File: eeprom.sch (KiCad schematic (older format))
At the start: 7 parts

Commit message: finalize schematic and PCB
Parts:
- added D3: LED, LED_SMD:LED_0603_1608Metric_Pad1.05x0.95mm_HandSolder, symbol Device:LED
- added D4: D_Schottky, Diode_SMD:D_0603_1608Metric_Pad1.05x0.95mm_HandSolder, symbol Device:D_Schottky
- added F2: Fuse, Fuse:Fuse_0603_1608Metric_Pad1.05x0.95mm_HandSolder, symbol Device:Fuse
- added R31: R, Resistor_SMD:R_0603_1608Metric_Pad1.05x0.95mm_HandSolder, symbol Device:R
- U10: renamed from U?; footprint Package_DFN_QFN:DFN-8-1EP_2x3mm_P0.5mm_EP0.61x2.2mm -> Package_DFN_QFN:DFN-8-1EP_3x2mm_P0.5mm_EP1.75x1.45mm
- gave numbers to parts that had none: 6
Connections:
- net labels added: 5V_IN_RAW
- net labels removed: 5V_IN
- wire segments 24 -> 29
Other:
- moved on the sheet: C35, R32, R33, R34, R35, R36, U10

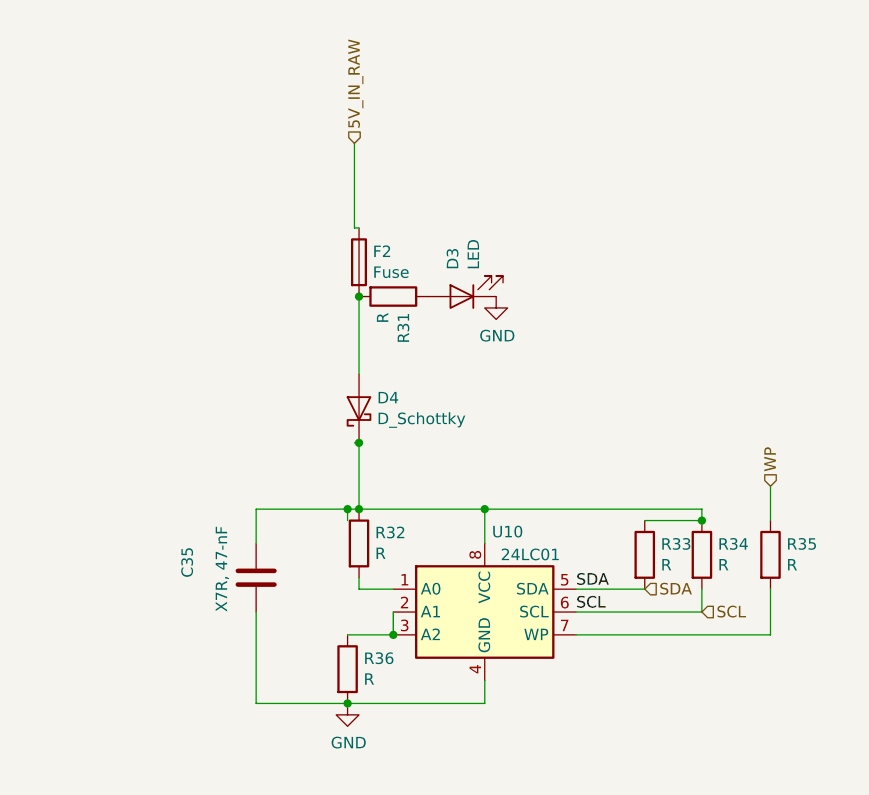
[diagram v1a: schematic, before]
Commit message: re route pcb-re arrange schematics
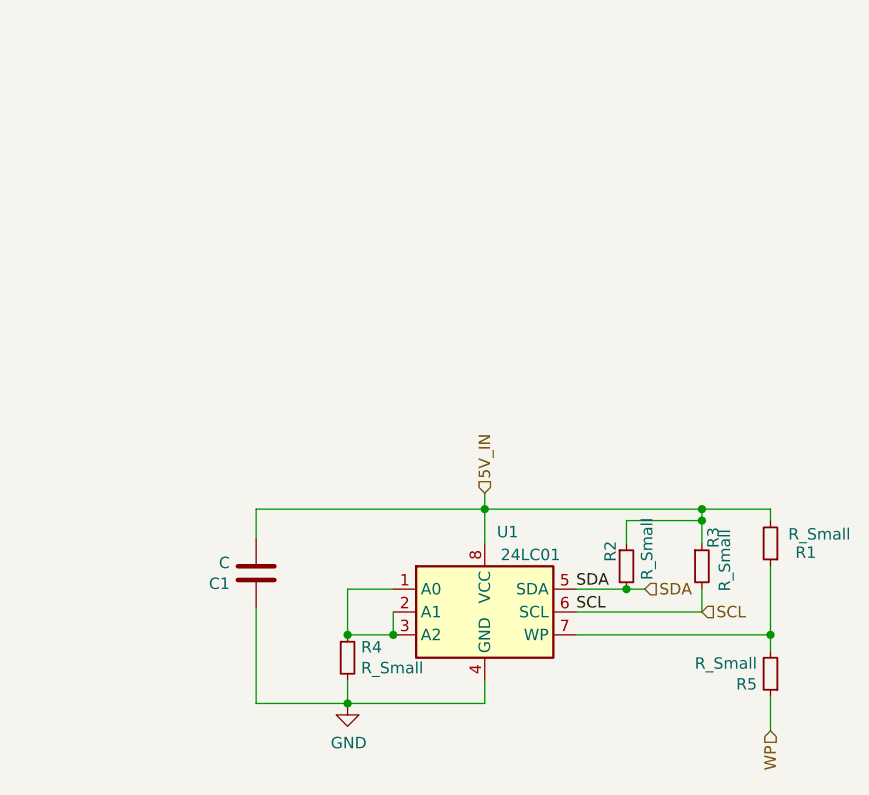
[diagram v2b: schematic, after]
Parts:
- removed C35: X7R, 47-nF, Capacitor_SMD:C_0603_1608Metric_Pad1.05x0.95mm_HandSolder, symbol Device:C
- removed D3: LED, LED_SMD:LED_0603_1608Metric_Pad1.05x0.95mm_HandSolder, symbol Device:LED
- removed D4: D_Schottky, Diode_SMD:D_0603_1608Metric_Pad1.05x0.95mm_HandSolder, symbol Device:D_Schottky
- removed F2: Fuse, Fuse:Fuse_0603_1608Metric_Pad1.05x0.95mm_HandSolder, symbol Device:Fuse
- removed R31, R32, R33, R34, R35, R36: R, Resistor_SMD:R_0603_1608Metric_Pad1.05x0.95mm_HandSolder, symbol Device:R
- added C1: C, Capacitor_SMD:C_0402_1005Metric, symbol Device:C
- added R1, R2, R3, R4, R5: R_Small, Resistor_SMD:R_0402_1005Metric, symbol Device:R_Small
- renumbered U10 to U1
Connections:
- net labels added: 5V_IN
- net labels removed: 5V_IN_RAW
- wire segments 29 -> 28
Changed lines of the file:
@@
 $Descr A4 11693 8268
 encoding utf-8
-Sheet 2 2
+Sheet 2 4
 Title ""
 Date ""
@@
 $EndDescr
 $Comp
-L Memory_EEPROM:24LC01 U10
+L Memory_EEPROM:24LC01 U1
 U 1 1 60F67DC6
 P 5000 4320
-F 0 "U10" H 5100 4670 50  0000 C CNN
+F 0 "U1" H 5100 4670 50  0000 C CNN
 F 1 "24LC01" H 5200 4570 50  0000 C CNN
 F 2 "Package_DFN_QFN:DFN-8-1EP_3x2mm_P0.5mm_EP1.75x1.45mm" H 5000 4320 50  0001 C CNN
@@
 	1    0    0    -1
 $EndComp
-$Comp
-L Device:R R32
-U 1 1 60F67DCC
-P 4450 4020
-F 0 "R32" H 4520 4066 50  0000 L CNN
-F 1 "R" H 4520 3975 50  0000 L CNN
-F 2 "Resistor_SMD:R_0603_1608Metric_Pad1.05x0.95mm_HandSolder" V 4380 4020 50  0001 C CNN
-F 3 "~" H 4450 4020 50  0001 C CNN
-	1    4450 4020
-	1    0    0    -1
-$EndComp
-Wire Wire Line
-	4600 4220 4450 4220
-Wire Wire Line
-	4450 4220 4450 4170
 Wire Wire Line
 	4600 4320 4600 4420
@@
 Connection ~ 4600 4420
 $Comp
-L Device:R R36
-U 1 1 60F67DD8
-P 4400 4570
-F 0 "R36" H 4470 4616 50  0000 L CNN
-F 1 "R" H 4470 4525 50  0000 L CNN
-F 2 "Resistor_SMD:R_0603_1608Metric_Pad1.05x0.95mm_HandSolder" V 4330 4570 50  0001 C CNN
-F 3 "~" H 4400 4570 50  0001 C CNN
-	1    4400 4570
-	1    0    0    -1
-$EndComp
-$Comp
-L power:GND #PWR020
+L power:GND #PWR01
 U 1 1 60F67DDE
 P 4400 4720
-F 0 "#PWR020" H 4400 4470 50  0001 C CNN
+F 0 "#PWR01" H 4400 4470 50  0001 C CNN
 F 1 "GND" H 4405 4547 50  0000 C CNN
 F 2 "" H 4400 4720 50  0001 C CNN
@@
 	1    0    0    -1
 $EndComp
-$Comp
-L Device:R R33
-U 1 1 60F67DE4
-P 5700 4070
-F 0 "R33" H 5770 4116 50  0000 L CNN
-F 1 "R" H 5770 4025 50  0000 L CNN
-F 2 "Resistor_SMD:R_0603_1608Metric_Pad1.05x0.95mm_HandSolder" V 5630 4070 50  0001 C CNN
-F 3 "~" H 5700 4070 50  0001 C CNN
-	1    5700 4070
-	1    0    0    -1
-$EndComp
-$Comp
-L Device:R R34
-U 1 1 60F67DEA
-P 5950 4070
-F 0 "R34" H 6020 4116 50  0000 L CNN
-F 1 "R" H 6020 4025 50  0000 L CNN
-F 2 "Resistor_SMD:R_0603_1608Metric_Pad1.05x0.95mm_HandSolder" V 5880 4070 50  0001 C CNN
-F 3 "~" H 5950 4070 50  0001 C CNN
-	1    5950 4070
-	1    0    0    -1
-$EndComp
 Wire Wire Line
-	5400 4220 5700 4220
+	5400 4220 5620 4220
 Wire Wire Line
 	5400 4320 5950 4320
 Wire Wire Line
 	5950 4320 5950 4220
-Connection ~ 5950 3920
-Wire Wire Line
-	5950 3920 5700 3920
-Wire Wire Line
-	4450 3870 5000 3870
-Wire Wire Line
-	5950 3870 5950 3920
-Connection ~ 4450 3870
-$Comp
-L Device:C C35
-U 1 1 60F67DF8
-P 4000 4170
-F 0 "C35" V 3700 4170 50  0000 L CNN
-F 1 "X7R, 47-nF" V 3850 4020 50  0000 L CNN
-F 2 "Capacitor_SMD:C_0603_1608Metric_Pad1.05x0.95mm_HandSolder" H 4038 4020 50  0001 C CNN
-F 3 "~" H 4000 4170 50  0001 C CNN
-	1    4000 4170
-	1    0    0    -1
-$EndComp
-Wire Wire Line
-	4400 3920 4400 3870
-Wire Wire Line
-	4400 3870 4450 3870
-Wire Wire Line
-	4000 4020 4000 3870
-Wire Wire Line
-	4000 3870 4400 3870
-Connection ~ 4400 3870
-Wire Wire Line
-	4000 4320 4000 4720
 Wire Wire Line
 	4000 4720 4400 4720
@@
 SCL
 Wire Wire Line
-	4450 3570 4450 3580
-$Comp
-L Device:R R35
-U 1 1 60F67E0E
-P 6250 4070
-F 0 "R35" H 6320 4116 50  0000 L CNN
-F 1 "R" H 6320 4025 50  0000 L CNN
-F 2 "Resistor_SMD:R_0603_1608Metric_Pad1.05x0.95mm_HandSolder" V 6180 4070 50  0001 C CNN
-F 3 "~" H 6250 4070 50  0001 C CNN
-	1    6250 4070
-	1    0    0    -1
-$EndComp
-Wire Wire Line
-	6250 4420 6250 4220
-Wire Wire Line
-	6250 3920 6250 3770
+	6250 4690 6250 4840
 Wire Wire Line
 	5400 4420 6250 4420
@@
 Text HLabel 5700 4220 2    50   Input ~ 0
 SDA
-Text HLabel 6250 3770 1    50   Input ~ 0
+Text HLabel 6250 4840 3    50   Input ~ 0
 WP
-Text HLabel 4430 2270 1    50   Input ~ 0
-5V_IN_RAW
 $Comp
-L Device:Fuse F2
-U 1 1 60F6C1F8
-P 4450 2790
-F 0 "F2" H 4510 2836 50  0000 L CNN
-F 1 "Fuse" H 4510 2745 50  0000 L CNN
-F 2 "Fuse:Fuse_0603_1608Metric_Pad1.05x0.95mm_HandSolder" V 4380 2790 50  0001 C CNN
-F 3 "~" H 4450 2790 50  0001 C CNN
-	1    4450 2790
+L Device:C C?
+U 1 1 61531F73
+P 4000 4150
+AR Path="/61531F73" Ref="C?"  Part="1"
+AR Path="/6121F53E/61531F73" Ref="C?"  Part="1"
+AR Path="/60F72524/61531F73" Ref="C1"  Part="1"
+F 0 "C1" H 3885 4104 50  0000 R CNN
+F 1 "C" H 3885 4195 50  0000 R CNN
+F 2 "Capacitor_SMD:C_0402_1005Metric" H 4038 4000 50  0001 C CNN
+F 3 "~" H 4000 4150 50  0001 C CNN
+	1    4000 4150
+	1    0    0    -1
+$EndComp
+Wire Wire Line
+	4000 4300 4000 4720
+Wire Wire Line
+	4000 3870 4000 4000
+$Comp
+L Device:R_Small R?
+U 1 1 61536BCA
+P 4400 4520
+AR Path="/6121F53E/61536BCA" Ref="R?"  Part="1"
+AR Path="/60F72524/61536BCA" Ref="R4"  Part="1"
+F 0 "R4" H 4459 4566 50  0000 L CNN
+F 1 "R_Small" H 4459 4475 50  0000 L CNN
+F 2 "Resistor_SMD:R_0402_1005Metric" H 4400 4520 50  0001 C CNN
+F 3 "~" H 4400 4520 50  0001 C CNN
+	1    4400 4520
+	1    0    0    -1
+$EndComp
+Wire Wire Line
+	4400 4620 4400 4720
+$Comp
+L Device:R_Small R?
+U 1 1 6153764D
+P 5620 4120
+AR Path="/6121F53E/6153764D" Ref="R?"  Part="1"
+AR Path="/60F72524/6153764D" Ref="R2"  Part="1"
+F 0 "R2" V 5550 4140 50  0000 L CNN
+F 1 "R_Small" V 5710 4060 50  0000 L CNN
+F 2 "Resistor_SMD:R_0402_1005Metric" H 5620 4120 50  0001 C CNN
+F 3 "~" H 5620 4120 50  0001 C CNN
+	1    5620 4120
+	1    0    0    -1
+$EndComp
+Connection ~ 5620 4220
+Wire Wire Line
+	5620 4220 5700 4220
+$Comp
+L Device:R_Small R?
+U 1 1 61537E1A
+P 5950 4120
+AR Path="/6121F53E/61537E1A" Ref="R?"  Part="1"
+AR Path="/60F72524/61537E1A" Ref="R3"  Part="1"
+F 0 "R3" V 6000 4200 50  0000 L CNN
+F 1 "R_Small" V 6050 4010 50  0000 L CNN
+F 2 "Resistor_SMD:R_0402_1005Metric" H 5950 4120 50  0001 C CNN
+F 3 "~" H 5950 4120 50  0001 C CNN
+	1    5950 4120
 	1    0    0    -1
 $EndComp
 $Comp
-L Device:R R31
-U 1 1 60F6CD7C
-P 4600 2940
-F 0 "R31" H 4670 2986 50  0000 L CNN
-F 1 "R" H 4670 2895 50  0000 L CNN
-F 2 "Resistor_SMD:R_0603_1608Metric_Pad1.05x0.95mm_HandSolder" V 4530 2940 50  0001 C CNN
-F 3 "~" H 4600 2940 50  0001 C CNN
-	1    4600 2940
-	0    1    1    0
-$EndComp
-$Comp
-L Device:LED D?
-U 1 1 60F70C87
-P 4900 2940
-AR Path="/60F70C87" Ref="D?"  Part="1"
-AR Path="/60F72524/60F70C87" Ref="D3"  Part="1"
-F 0 "D3" V 4939 2823 50  0000 R CNN
-F 1 "LED" V 4848 2823 50  0000 R CNN
-F 2 "LED_SMD:LED_0603_1608Metric_Pad1.05x0.95mm_HandSolder" H 4900 2940 50  0001 C CNN
-F 3 "~" H 4900 2940 50  0001 C CNN
-	1    4900 2940
+L Device:R_Small R?
+U 1 1 615385CC
+P 6250 4590
+AR Path="/6121F53E/615385CC" Ref="R?"  Part="1"
+AR Path="/60F72524/615385CC" Ref="R5"  Part="1"
+F 0 "R5" H 6309 4636 50  0000 L CNN
+F 1 "R_Small" H 6309 4545 50  0000 L CNN
+F 2 "Resistor_SMD:R_0402_1005Metric" H 6250 4590 50  0001 C CNN
+F 3 "~" H 6250 4590 50  0001 C CNN
+	1    6250 4590
 	-1   0    0    1
 $EndComp
+Wire Wire Line
+	5620 3920 5620 4020
+Wire Wire Line
+	5620 3920 5950 3920
+Wire Wire Line
+	6250 4120 6250 4420
+Wire Wire Line
+	5950 3870 5950 3920
+Connection ~ 5950 3920
+Wire Wire Line
+	5950 3920 5950 4020
+Wire Wire Line
+	6250 4420 6250 4490
+Connection ~ 6250 4420
 $Comp
-L power:GND #PWR019
-U 1 1 60F70EE9
-P 5050 2940
-F 0 "#PWR019" H 5050 2690 50  0001 C CNN
-F 1 "GND" H 5055 2767 50  0000 C CNN
-F 2 "" H 5050 2940 50  0001 C CNN
-F 3 "" H 5050 2940 50  0001 C CNN
-	1    5050 2940
-	1    0    0    -1
+L Device:R_Small R?
+U 1 1 6153C7AE
+P 6250 4020
+AR Path="/6121F53E/6153C7AE" Ref="R?"  Part="1"
+AR Path="/60F72524/6153C7AE" Ref="R1"  Part="1"
+F 0 "R1" H 6050 4060 50  0000 L CNN
+F 1 "R_Small" H 5900 3980 50  0000 L CNN
+F 2 "Resistor_SMD:R_0402_1005Metric" H 6250 4020 50  0001 C CNN
+F 3 "~" H 6250 4020 50  0001 C CNN
+	1    6250 4020
+	-1   0    0    1
 $EndComp
 Wire Wire Line
-	4450 2940 4450 3280
+	5950 3870 6250 3870
 Wire Wire Line
-	4430 3580 4450 3580
-Connection ~ 4450 2940
-Connection ~ 4450 3580
+	6250 3870 6250 3920
+Connection ~ 5950 3870
 Wire Wire Line
-	4450 3580 4450 3870
-$Comp
-L Device:D_Schottky D4
-U 1 1 60F73875
-P 4450 3430
-F 0 "D4" V 4496 3351 50  0000 R CNN
-F 1 "D_Schottky" V 4405 3351 50  0000 R CNN
-F 2 "Diode_SMD:D_0603_1608Metric_Pad1.05x0.95mm_HandSolder" H 4450 3430 50  0001 C CNN
-F 3 "~" H 4450 3430 50  0001 C CNN
-	1    4450 3430
-	0    -1   -1   0
-$EndComp
+	4400 4220 4400 4420
 Wire Wire Line
-	4430 2270 4430 2640
+	4400 4220 4600 4220
+Connection ~ 4400 4420
 Wire Wire Line
-	4430 2640 4450 2640
+	4000 3870 5000 3870
+Text HLabel 5000 3800 1    50   Input ~ 0
+5V_IN
+Wire Wire Line
+	5000 3800 5000 3870
 $EndSCHEMATC

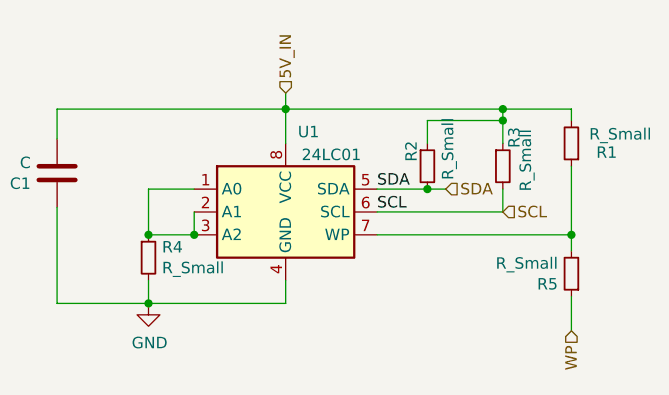
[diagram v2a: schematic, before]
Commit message: update eeprom resistor values
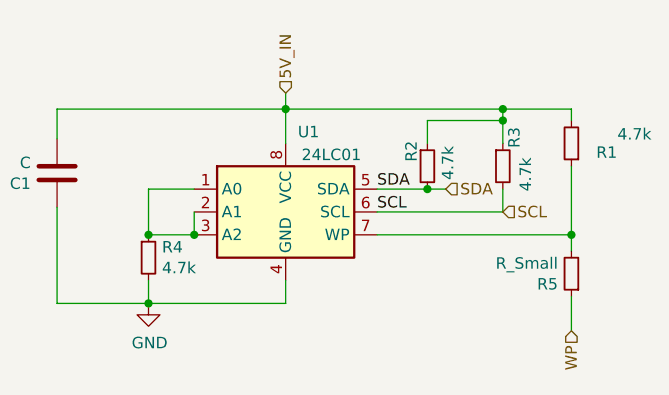
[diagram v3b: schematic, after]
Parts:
- R1, R2, R3, R4: value R_Small -> 4.7k
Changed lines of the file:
@@
 AR Path="/60F72524/61536BCA" Ref="R4"  Part="1"
 F 0 "R4" H 4459 4566 50  0000 L CNN
-F 1 "R_Small" H 4459 4475 50  0000 L CNN
+F 1 "4.7k" H 4459 4475 50  0000 L CNN
 F 2 "Resistor_SMD:R_0402_1005Metric" H 4400 4520 50  0001 C CNN
 F 3 "~" H 4400 4520 50  0001 C CNN
@@
 AR Path="/60F72524/6153764D" Ref="R2"  Part="1"
 F 0 "R2" V 5550 4140 50  0000 L CNN
-F 1 "R_Small" V 5710 4060 50  0000 L CNN
+F 1 "4.7k" V 5710 4060 50  0000 L CNN
 F 2 "Resistor_SMD:R_0402_1005Metric" H 5620 4120 50  0001 C CNN
 F 3 "~" H 5620 4120 50  0001 C CNN
@@
 AR Path="/60F72524/61537E1A" Ref="R3"  Part="1"
 F 0 "R3" V 6000 4200 50  0000 L CNN
-F 1 "R_Small" V 6050 4010 50  0000 L CNN
+F 1 "4.7k" V 6050 4010 50  0000 L CNN
 F 2 "Resistor_SMD:R_0402_1005Metric" H 5950 4120 50  0001 C CNN
 F 3 "~" H 5950 4120 50  0001 C CNN
@@
 AR Path="/60F72524/6153C7AE" Ref="R1"  Part="1"
 F 0 "R1" H 6050 4060 50  0000 L CNN
-F 1 "R_Small" H 5900 3980 50  0000 L CNN
+F 1 "4.7k" H 5900 3980 50  0000 L CNN
 F 2 "Resistor_SMD:R_0402_1005Metric" H 6250 4020 50  0001 C CNN
 F 3 "~" H 6250 4020 50  0001 C CNN
